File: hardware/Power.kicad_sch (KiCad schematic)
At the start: 70 parts, among them J10 I2C, J3 ESTOP, J4 PWR, J5 Conn_ARM_JTAG_SWD_10, J7 FAN, J9 DEBUG, Q1 MMBT5401LT1G, Q2 PSMN4R8-100BSEJ, Q3 MMBT3904, Q5 PSMN4R8-100BSEJ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

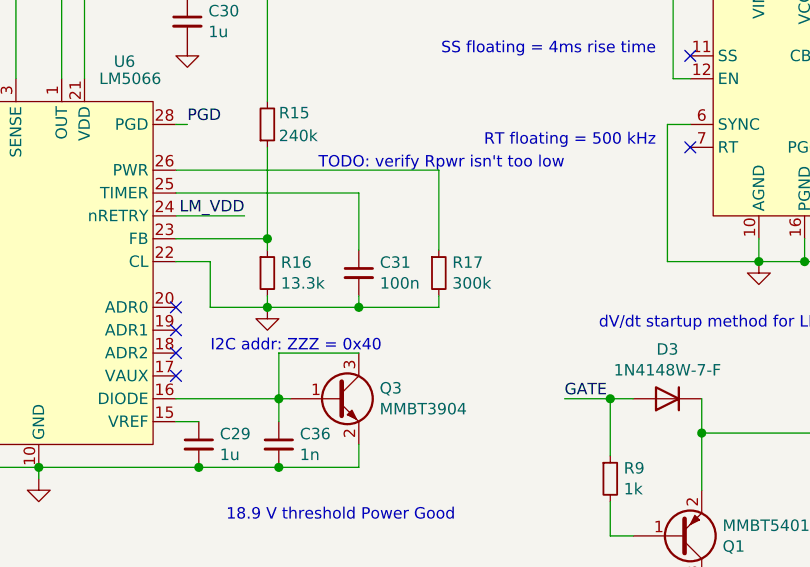
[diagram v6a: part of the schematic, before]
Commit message: Adjusting Timer (C31)
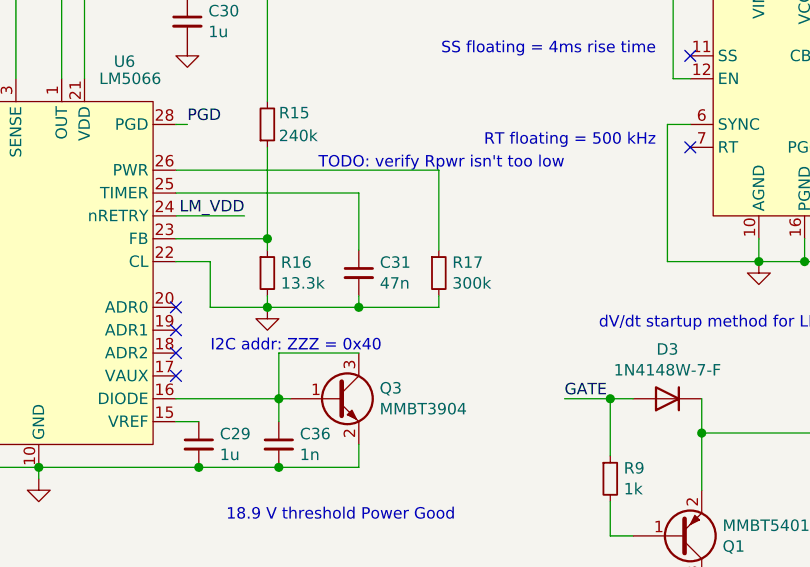
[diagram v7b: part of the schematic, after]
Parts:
- C31: value 100n -> 47n; D1PN 311-1344-1-ND -> 1276-2070-2-ND; MFN Yageo -> Samsung Electro-Mechanics; MPN CC0603KRX7R9BB104 -> CL10B473JB8NNNC
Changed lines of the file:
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@@
       (effects (font (size 1.27 1.27)) (justify left))
     )
-    (property "Value" "100n" (id 1) (at 143.3068 70.993 0)
+    (property "Value" "47n" (id 1) (at 143.3068 70.993 0)
       (effects (font (size 1.27 1.27)) (justify left))
     )
@@
       (effects (font (size 1.27 1.27)) hide)
     )
-    (property "D1PN" "311-1344-1-ND" (id 5) (at 143.3068 66.1416 0)
+    (property "D1PN" "1276-2070-2-ND" (id 5) (at 143.3068 66.1416 0)
       (effects (font (size 1.27 1.27)) hide)
     )
-    (property "MFN" "Yageo" (id 6) (at 143.3068 66.1416 0)
+    (property "MFN" "Samsung Electro-Mechanics" (id 6) (at 143.3068 66.1416 0)
       (effects (font (size 1.27 1.27)) hide)
     )
-    (property "MPN" "CC0603KRX7R9BB104" (id 7) (at 143.3068 66.1416 0)
+    (property "MPN" "CL10B473JB8NNNC" (id 7) (at 143.3068 66.1416 0)
       (effects (font (size 1.27 1.27)) hide)
     )
